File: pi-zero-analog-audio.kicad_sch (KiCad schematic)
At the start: 31 parts, among them J1 GPIO, J2 Screw_Terminal_01x04, J3 SJ1-3555NG-BE, U1 MIC5365-3.3YD5, U2 MC74VHC1GT50, U3 MC74VHC1GT50, U4 PAM8403D

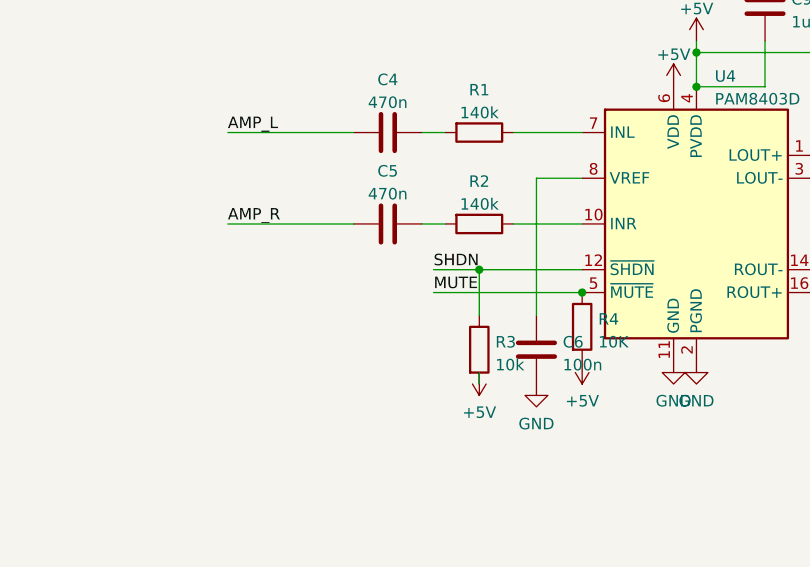
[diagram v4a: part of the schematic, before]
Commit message: Adding SolderJumpers for GPIO connections
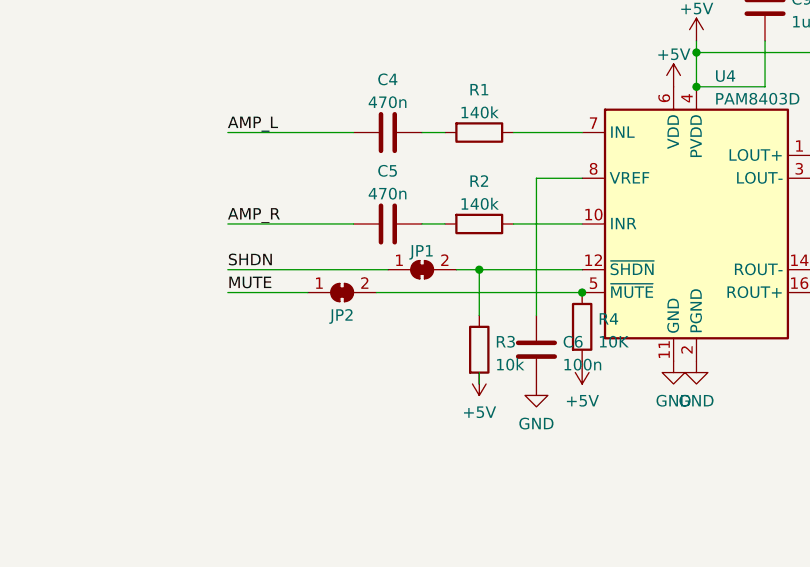
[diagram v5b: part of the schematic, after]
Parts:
- added JP1, JP2: SolderJumper_2_Bridged, Jumper:SolderJumper-2_P1.3mm_Bridged_RoundedPad1.0x1.5mm, symbol Jumper:SolderJumper_2_Bridged
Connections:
- net MUTE: now also JP2.1 (A); no longer R4.1, U4.5 (~{MUTE})
- net SHDN: now also JP1.1 (A); no longer R3.1, U4.12 (~{SHDN})
- new net: JP1.2 (B), R3.1, U4.12 (~{SHDN})
- new net: JP2.2 (B), R4.1, U4.5 (~{MUTE})
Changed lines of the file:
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@@
+    (stroke (width 0) (type default) (color 0 0 0 0))
+  )
+  (wire (pts (xy 101.6 134.62) (xy 104.14 134.62))
     (stroke (width 0) (type default) (color 0 0 0 0))
   )
@@
     (stroke (width 0) (type default) (color 0 0 0 0))
   )
-  (wire (pts (xy 99.06 137.16) (xy 115.57 137.16))
+  (wire (pts (xy 76.2 137.16) (xy 85.09 137.16))
     (stroke (width 0) (type default) (color 0 0 0 0))
   )
@@
     (stroke (width 0) (type solid) (color 0 0 0 0))
   )
-  (wire (pts (xy 99.06 134.62) (xy 104.14 134.62))
+  (wire (pts (xy 92.71 137.16) (xy 115.57 137.16))
+    (stroke (width 0) (type default) (color 0 0 0 0))
+  )
+  (wire (pts (xy 76.2 134.62) (xy 93.98 134.62))
     (stroke (width 0) (type default) (color 0 0 0 0))
   )
@@
     (effects (font (size 1.27 1.27)) (justify left bottom))
   )
-  (label "SHDN" (at 99.06 134.62 0)
+  (label "SHDN" (at 76.2 134.62 0)
     (effects (font (size 1.27 1.27)) (justify left bottom))
   )
@@
     (effects (font (size 1.27 1.27)) (justify left bottom))
   )
-  (label "MUTE" (at 99.06 137.16 0)
+  (label "MUTE" (at 76.2 137.16 0)
     (effects (font (size 1.27 1.27)) (justify left bottom))
   )
@@
   (symbol (lib_id "power:GND") (at 142.24 38.1 0) (unit 1)
     (in_bom yes) (on_board yes) (fields_autoplaced)
-    (property "Reference" "#PWR021" (id 0) (at 142.24 44.45 0)
+    (property "Reference" "#PWR022" (id 0) (at 142.24 44.45 0)
       (effects (font (size 1.27 1.27)) hide)
     )
@@
     (pin "1")
   )
+  (symbol (lib_id "Jumper:SolderJumper_2_Bridged") (at 97.79 134.62 0) (unit 1)
+    (in_bom yes) (on_board yes) (fields_autoplaced)
+    (property "Reference" "JP1" (id 0) (at 97.79 132.5682 0))
+    (property "Value" "SolderJumper_2_Bridged" (id 1) (at 97.79 132.5681 0)
+      (effects (font (size 1.27 1.27)) hide)
+    )
+    (property "Footprint" "Jumper:SolderJumper-2_P1.3mm_Bridged_RoundedPad1.0x1.5mm" (id 2) (at 97.79 134.62 0)
+      (effects (font (size 1.27 1.27)) hide)
+    )
+    (property "Datasheet" "~" (id 3) (at 97.79 134.62 0)
+      (effects (font (size 1.27 1.27)) hide)
+    )
+    (pin "1")
+    (pin "2")
+  )
   (symbol (lib_id "Device:C") (at 121.92 72.39 0) (unit 1)
     (in_bom yes) (on_board yes) (fields_autoplaced)
@@
   (symbol (lib_id "power:GND") (at 128.27 144.78 0) (unit 1)
     (in_bom yes) (on_board yes) (fields_autoplaced)
-    (property "Reference" "#PWR019" (id 0) (at 128.27 151.13 0)
+    (property "Reference" "#PWR020" (id 0) (at 128.27 151.13 0)
       (effects (font (size 1.27 1.27)) hide)
     )
@@
   (symbol (lib_id "power:+5V") (at 125.73 114.3 0) (unit 1)
     (in_bom yes) (on_board yes) (fields_autoplaced)
-    (property "Reference" "#PWR016" (id 0) (at 125.73 118.11 0)
+    (property "Reference" "#PWR017" (id 0) (at 125.73 118.11 0)
       (effects (font (size 1.27 1.27)) hide)
     )
@@
   (symbol (lib_id "power:+5V") (at 128.27 109.22 0) (unit 1)
     (in_bom yes) (on_board yes) (fields_autoplaced)
-    (property "Reference" "#PWR018" (id 0) (at 128.27 113.03 0)
+    (property "Reference" "#PWR019" (id 0) (at 128.27 113.03 0)
       (effects (font (size 1.27 1.27)) hide)
     )
@@
   (symbol (lib_id "power:GND") (at 201.93 41.91 0) (unit 1)
     (in_bom yes) (on_board yes) (fields_autoplaced)
-    (property "Reference" "#PWR026" (id 0) (at 201.93 48.26 0)
+    (property "Reference" "#PWR027" (id 0) (at 201.93 48.26 0)
       (effects (font (size 1.27 1.27)) hide)
     )
@@
   (symbol (lib_id "power:GND") (at 143.51 101.6 180) (unit 1)
     (in_bom yes) (on_board yes) (fields_autoplaced)
-    (property "Reference" "#PWR023" (id 0) (at 143.51 95.25 0)
+    (property "Reference" "#PWR024" (id 0) (at 143.51 95.25 0)
       (effects (font (size 1.27 1.27)) hide)
     )
@@
   (symbol (lib_id "power:GND") (at 143.51 73.66 0) (unit 1)
     (in_bom yes) (on_board yes) (fields_autoplaced)
-    (property "Reference" "#PWR022" (id 0) (at 143.51 80.01 0)
+    (property "Reference" "#PWR023" (id 0) (at 143.51 80.01 0)
       (effects (font (size 1.27 1.27)) hide)
     )
@@
   (symbol (lib_id "power:GND") (at 135.89 101.6 180) (unit 1)
     (in_bom yes) (on_board yes) (fields_autoplaced)
-    (property "Reference" "#PWR020" (id 0) (at 135.89 95.25 0)
+    (property "Reference" "#PWR021" (id 0) (at 135.89 95.25 0)
       (effects (font (size 1.27 1.27)) hide)
     )
@@
   (symbol (lib_id "power:GND") (at 161.29 73.66 0) (unit 1)
     (in_bom yes) (on_board yes) (fields_autoplaced)
-    (property "Reference" "#PWR025" (id 0) (at 161.29 80.01 0)
+    (property "Reference" "#PWR026" (id 0) (at 161.29 80.01 0)
       (effects (font (size 1.27 1.27)) hide)
     )
@@
   (symbol (lib_id "power:GND") (at 160.02 38.1 0) (unit 1)
     (in_bom yes) (on_board yes) (fields_autoplaced)
-    (property "Reference" "#PWR024" (id 0) (at 160.02 44.45 0)
+    (property "Reference" "#PWR025" (id 0) (at 160.02 44.45 0)
       (effects (font (size 1.27 1.27)) hide)
     )
@@
   (symbol (lib_id "power:GND") (at 125.73 144.78 0) (unit 1)
     (in_bom yes) (on_board yes) (fields_autoplaced)
-    (property "Reference" "#PWR017" (id 0) (at 125.73 151.13 0)
+    (property "Reference" "#PWR018" (id 0) (at 125.73 151.13 0)
       (effects (font (size 1.27 1.27)) hide)
     )
@@
     )
     (pin "1")
+  )
+  (symbol (lib_id "Jumper:SolderJumper_2_Bridged") (at 88.9 137.16 0) (unit 1)
+    (in_bom yes) (on_board yes)
+    (property "Reference" "JP2" (id 0) (at 88.9 139.7 0))
+    (property "Value" "SolderJumper_2_Bridged" (id 1) (at 88.9 135.1081 0)
+      (effects (font (size 1.27 1.27)) hide)
+    )
+    (property "Footprint" "Jumper:SolderJumper-2_P1.3mm_Bridged_RoundedPad1.0x1.5mm" (id 2) (at 88.9 137.16 0)
+      (effects (font (size 1.27 1.27)) hide)
+    )
+    (property "Datasheet" "~" (id 3) (at 88.9 137.16 0)
+      (effects (font (size 1.27 1.27)) hide)
+    )
+    (pin "1")
+    (pin "2")
   )
   (symbol (lib_id "Logic_LevelTranslator:SN74LV1T34DBV") (at 110.49 66.04 0) (unit 1)
@@
   (symbol (lib_id "power:GND") (at 121.92 76.2 0) (unit 1)
     (in_bom yes) (on_board yes) (fields_autoplaced)
-    (property "Reference" "#PWR0101" (id 0) (at 121.92 82.55 0)
+    (property "Reference" "#PWR016" (id 0) (at 121.92 82.55 0)
       (effects (font (size 1.27 1.27)) hide)
     )
@@
       (reference "#PWR015") (unit 1) (value "GND") (footprint "")
     )
+    (path "/ffede39b-8099-4955-86bd-53060798d5f3"
+      (reference "#PWR016") (unit 1) (value "GND") (footprint "")
+    )
     (path "/4da06035-fff1-4a29-81dd-8f4dbe59fff0"
-      (reference "#PWR016") (unit 1) (value "+5V") (footprint "")
+      (reference "#PWR017") (unit 1) (value "+5V") (footprint "")
     )
     (path "/e95beca7-444a-4cc5-9f40-709df3f136ab"
-      (reference "#PWR017") (unit 1) (value "GND") (footprint "")
+      (reference "#PWR018") (unit 1) (value "GND") (footprint "")
     )
     (path "/53e9b269-f0a7-47e4-af71-77298a928f0e"
-      (reference "#PWR018") (unit 1) (value "+5V") (footprint "")
+      (reference "#PWR019") (unit 1) (value "+5V") (footprint "")
     )
     (path "/4b95a9c2-acb6-4774-a3c3-7825fc03dabe"
-      (reference "#PWR019") (unit 1) (value "GND") (footprint "")
+      (reference "#PWR020") (unit 1) (value "GND") (footprint "")
     )
     (path "/b7024d58-cd8d-42b0-8d27-e41166a9a27b"
-      (reference "#PWR020") (unit 1) (value "GND") (footprint "")
+      (reference "#PWR021") (unit 1) (value "GND") (footprint "")
     )
     (path "/10e102fd-a91f-4c41-9a82-8c538dc349c6"
-      (reference "#PWR021") (unit 1) (value "GND") (footprint "")
+      (reference "#PWR022") (unit 1) (value "GND") (footprint "")
     )
     (path "/a31e2c62-695d-402d-aace-8193a0330673"
-      (reference "#PWR022") (unit 1) (value "GND") (footprint "")
+      (reference "#PWR023") (unit 1) (value "GND") (footprint "")
     )
     (path "/9efb607d-91e6-407b-8efc-00809228de63"
-      (reference "#PWR023") (unit 1) (value "GND") (footprint "")
+      (reference "#PWR024") (unit 1) (value "GND") (footprint "")
     )
     (path "/e13487f4-f7e8-42a5-aaa9-41aa8c3edf07"
-      (reference "#PWR024") (unit 1) (value "GND") (footprint "")
+      (reference "#PWR025") (unit 1) (value "GND") (footprint "")
     )
     (path "/d4eceaab-1d31-4003-bead-a40555a1f2ed"
-      (reference "#PWR025") (unit 1) (value "GND") (footprint "")
+      (reference "#PWR026") (unit 1) (value "GND") (footprint "")
     )
     (path "/78668128-17e5-44d7-9944-cfbf5034c0d3"
-      (reference "#PWR026") (unit 1) (value "GND") (footprint "")
-    )
-    (path "/ffede39b-8099-4955-86bd-53060798d5f3"
-      (reference "#PWR0101") (unit 1) (value "GND") (footprint "")
+      (reference "#PWR027") (unit 1) (value "GND") (footprint "")
     )
     (path "/e0d29500-3eeb-41c8-beba-a4e29bee1456"
@@
       (reference "J3") (unit 1) (value "SJ1-3555NG-BE") (footprint "library:CUI_SJ1-3555NG-BE")
     )
+    (path "/42de515a-bd7a-4b70-9fe9-9e1aed3ae372"
+      (reference "JP1") (unit 1) (value "SolderJumper_2_Bridged") (footprint "Jumper:SolderJumper-2_P1.3mm_Bridged_RoundedPad1.0x1.5mm")
+    )
+    (path "/ebb81792-e83d-4c58-b4ba-3ae00249565c"
+      (reference "JP2") (unit 1) (value "SolderJumper_2_Bridged") (footprint "Jumper:SolderJumper-2_P1.3mm_Bridged_RoundedPad1.0x1.5mm")
+    )
     (path "/d084b509-2bd2-4510-bb62-a6e63bec94c3"

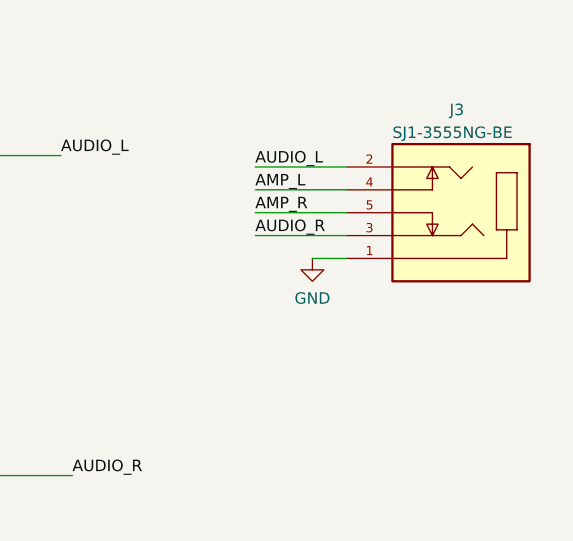
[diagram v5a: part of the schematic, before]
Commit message: Changing audio connector reference and footprint
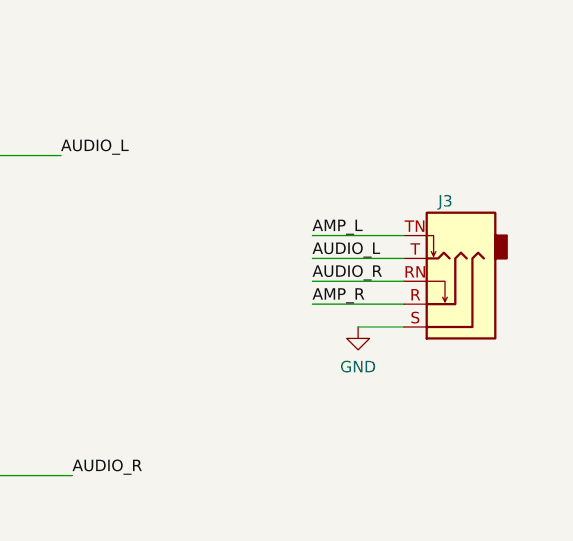
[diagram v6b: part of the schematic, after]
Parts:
- J3: value SJ1-3555NG-BE -> Audio Jack; footprint library:CUI_SJ1-3555NG-BE -> Connector_Audio:Jack_3.5mm_Ledino_KB3SPRS_Horizontal; symbol SJ1-3555NG-BE:SJ1-3555NG-BE -> Connector:AudioJack3_SwitchTR
- U1: footprint Package_TO_SOT_SMD:SOT-23-5 -> Package_TO_SOT_SMD:SOT-23-5_HandSoldering
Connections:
- net AMP_L: now also J3.TN; no longer J3.4
- net AMP_R: now also J3.R; no longer J3.5
- net AUDIO_L: now also J3.T; no longer J3.2
- net AUDIO_R: now also J3.RN; no longer J3.3
- net GND: now also J3.S; no longer J3.1
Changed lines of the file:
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@@
     (stroke (width 0) (type solid) (color 0 0 0 0))
   )
-  (wire (pts (xy 195.58 36.83) (xy 205.74 36.83))
+  (wire (pts (xy 201.93 46.99) (xy 212.09 46.99))
     (stroke (width 0) (type default) (color 0 0 0 0))
   )
@@
     (stroke (width 0) (type solid) (color 0 0 0 0))
   )
+  (wire (pts (xy 207.01 49.53) (xy 212.09 49.53))
+    (stroke (width 0) (type default) (color 0 0 0 0))
+  )
   (wire (pts (xy 87.63 30.48) (xy 87.63 33.02))
     (stroke (width 0) (type default) (color 0 0 0 0))
@@
     (stroke (width 0) (type default) (color 0 0 0 0))
   )
-  (wire (pts (xy 195.58 31.75) (xy 205.74 31.75))
+  (wire (pts (xy 201.93 41.91) (xy 212.09 41.91))
     (stroke (width 0) (type default) (color 0 0 0 0))
   )
@@
     (stroke (width 0) (type default) (color 0 0 0 0))
   )
-  (wire (pts (xy 195.58 39.37) (xy 205.74 39.37))
+  (wire (pts (xy 201.93 44.45) (xy 212.09 44.45))
     (stroke (width 0) (type default) (color 0 0 0 0))
   )
@@
     (stroke (width 0) (type default) (color 0 0 0 0))
   )
-  (wire (pts (xy 195.58 34.29) (xy 205.74 34.29))
+  (wire (pts (xy 201.93 39.37) (xy 212.09 39.37))
     (stroke (width 0) (type default) (color 0 0 0 0))
   )
@@
     (stroke (width 0) (type default) (color 0 0 0 0))
   )
-  (wire (pts (xy 205.74 41.91) (xy 201.93 41.91))
-    (stroke (width 0) (type default) (color 0 0 0 0))
-  )
   (text "Additional pin functions:\nhttps://pinout.xyz/" (at 179.07 180.34 0)
     (effects (font (size 1.27 1.27)) (justify left bottom))
@@
     (effects (font (size 1.27 1.27)) (justify left bottom))
   )
-  (label "AUDIO_R" (at 195.58 39.37 0)
+  (label "AUDIO_R" (at 201.93 44.45 0)
     (effects (font (size 1.27 1.27)) (justify left bottom))
   )
@@
     (effects (font (size 1.27 1.27)) (justify left bottom))
   )
-  (label "AMP_R" (at 195.58 36.83 0)
+  (label "AMP_R" (at 201.93 46.99 0)
     (effects (font (size 1.27 1.27)) (justify left bottom))
   )
@@
     (effects (font (size 1.27 1.27)) (justify left bottom))
   )
-  (label "AMP_L" (at 195.58 34.29 0)
+  (label "AMP_L" (at 201.93 39.37 0)
     (effects (font (size 1.27 1.27)) (justify left bottom))
   )
@@
     (effects (font (size 1.27 1.27)) (justify left bottom))
   )
-  (label "AUDIO_L" (at 195.58 31.75 0)
+  (label "AUDIO_L" (at 201.93 41.91 0)
     (effects (font (size 1.27 1.27)) (justify left bottom))
   )
@@
     (pin "2")
   )
-  (symbol (lib_id "SJ1-3555NG-BE:SJ1-3555NG-BE") (at 218.44 36.83 180) (unit 1)
+  (symbol (lib_id "Connector:AudioJack3_SwitchTR") (at 217.17 46.99 180) (unit 1)
     (in_bom yes) (on_board yes)
-    (property "Reference" "J3" (id 0) (at 217.17 25.4 0)
+    (property "Reference" "J3" (id 0) (at 215.9 35.56 0)
       (effects (font (size 1.27 1.27)) (justify right))
     )
-    (property "Value" "SJ1-3555NG-BE" (id 1) (at 210.82 27.94 0)
-      (effects (font (size 1.27 1.27)) (justify right))
-    )
-    (property "Footprint" "library:CUI_SJ1-3555NG-BE" (id 2) (at 218.44 36.83 0)
+    (property "Value" "Audio Jack" (id 1) (at 212.09 38.1 0)
+      (effects (font (size 1.27 1.27)) (justify right) hide)
+    )
+    (property "Footprint" "Connector_Audio:Jack_3.5mm_Ledino_KB3SPRS_Horizontal" (id 2) (at 217.17 46.99 0)
+      (effects (font (size 1.27 1.27)) hide)
+    )
+    (property "Datasheet" "~" (id 3) (at 217.17 46.99 0)
+      (effects (font (size 1.27 1.27)) hide)
+    )
+    (property "MANUFACTURER" "CUI Devices" (id 4) (at 217.17 46.99 0)
       (effects (font (size 1.27 1.27)) (justify left bottom) hide)
     )
-    (property "Datasheet" "" (id 3) (at 218.44 36.83 0)
+    (property "PART_REV" "1.0" (id 5) (at 217.17 46.99 0)
       (effects (font (size 1.27 1.27)) (justify left bottom) hide)
     )
-    (property "MANUFACTURER" "CUI Devices" (id 4) (at 218.44 36.83 0)
+    (property "SNAPEDA_PN" "SJ1-3555NG-BE" (id 6) (at 217.17 46.99 0)
       (effects (font (size 1.27 1.27)) (justify left bottom) hide)
     )
-    (property "PART_REV" "1.0" (id 5) (at 218.44 36.83 0)
+    (property "STANDARD" "Manufacturer Recommendation" (id 7) (at 217.17 46.99 0)
       (effects (font (size 1.27 1.27)) (justify left bottom) hide)
     )
-    (property "SNAPEDA_PN" "SJ1-3555NG-BE" (id 6) (at 218.44 36.83 0)
+    (property "MAXIMUM_PACKAGE_HEIGHT" "10.3 mm" (id 8) (at 217.17 46.99 0)
       (effects (font (size 1.27 1.27)) (justify left bottom) hide)
     )
-    (property "STANDARD" "Manufacturer Recommendation" (id 7) (at 218.44 36.83 0)
-      (effects (font (size 1.27 1.27)) (justify left bottom) hide)
-    )
-    (property "MAXIMUM_PACKAGE_HEIGHT" "10.3 mm" (id 8) (at 218.44 36.83 0)
-      (effects (font (size 1.27 1.27)) (justify left bottom) hide)
-    )
-    (pin "1")
-    (pin "2")
-    (pin "3")
-    (pin "4")
-    (pin "5")
+    (pin "R")
+    (pin "RN")
+    (pin "S")
+    (pin "T")
+    (pin "TN")
   )
   (symbol (lib_id "Device:R") (at 160.02 34.29 0) (unit 1)
@@
     (pin "2")
   )
-  (symbol (lib_id "power:GND") (at 201.93 41.91 0) (unit 1)
-    (in_bom yes) (on_board yes) (fields_autoplaced)
-    (property "Reference" "#PWR027" (id 0) (at 201.93 48.26 0)
-      (effects (font (size 1.27 1.27)) hide)
-    )
-    (property "Value" "GND" (id 1) (at 201.93 46.3534 0))
-    (property "Footprint" "" (id 2) (at 201.93 41.91 0)
-      (effects (font (size 1.27 1.27)) hide)
-    )
-    (property "Datasheet" "" (id 3) (at 201.93 41.91 0)
+  (symbol (lib_id "power:GND") (at 207.01 49.53 0) (unit 1)
+    (in_bom yes) (on_board yes) (fields_autoplaced)
+    (property "Reference" "#PWR027" (id 0) (at 207.01 55.88 0)
+      (effects (font (size 1.27 1.27)) hide)
+    )
+    (property "Value" "GND" (id 1) (at 207.01 53.9734 0))
+    (property "Footprint" "" (id 2) (at 207.01 49.53 0)
+      (effects (font (size 1.27 1.27)) hide)
+    )
+    (property "Datasheet" "" (id 3) (at 207.01 49.53 0)
       (effects (font (size 1.27 1.27)) hide)
     )
@@
     (property "Reference" "U1" (id 0) (at 72.39 24.2402 0))
     (property "Value" "MIC5365-3.3YD5" (id 1) (at 72.39 26.7771 0))
-    (property "Footprint" "Package_TO_SOT_SMD:SOT-23-5" (id 2) (at 72.39 24.13 0)
+    (property "Footprint" "Package_TO_SOT_SMD:SOT-23-5_HandSoldering" (id 2) (at 72.39 24.13 0)
       (effects (font (size 1.27 1.27)) hide)
     )
@@
     )
     (path "/0b4362dd-e0ca-493b-8fc1-107bd0984034"
-      (reference "J3") (unit 1) (value "SJ1-3555NG-BE") (footprint "library:CUI_SJ1-3555NG-BE")
+      (reference "J3") (unit 1) (value "Audio Jack") (footprint "Connector_Audio:Jack_3.5mm_Ledino_KB3SPRS_Horizontal")
     )
     (path "/42de515a-bd7a-4b70-9fe9-9e1aed3ae372"
@@
     )
     (path "/8e6d6488-458c-4211-a3e8-dc13acff85e7"
-      (reference "U1") (unit 1) (value "MIC5365-3.3YD5") (footprint "Package_TO_SOT_SMD:SOT-23-5")
+      (reference "U1") (unit 1) (value "MIC5365-3.3YD5") (footprint "Package_TO_SOT_SMD:SOT-23-5_HandSoldering")
     )
     (path "/a8cd6fe4-3274-461b-a92b-74b79798d756"

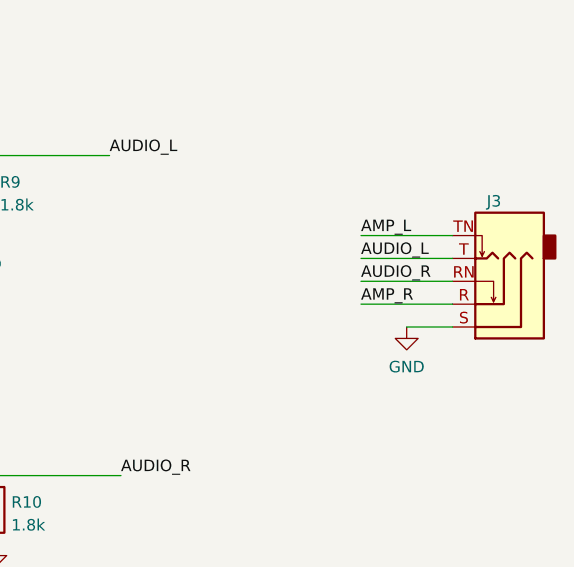
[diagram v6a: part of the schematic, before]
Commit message: Fix error in audio jack
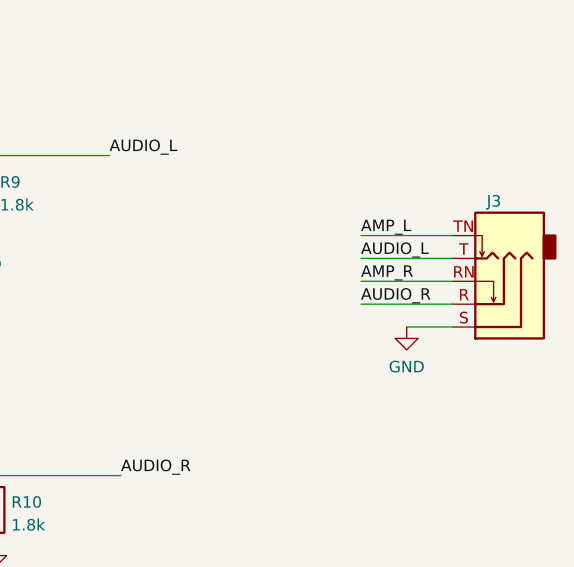
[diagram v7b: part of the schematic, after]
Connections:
- net AMP_R: now also J3.RN; no longer J3.R
- net AUDIO_R: now also J3.R; no longer J3.RN
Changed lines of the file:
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@@
-    (effects (font (size 1.27 1.27)) (justify left bottom))
-  )
-  (label "AUDIO_R" (at 201.93 44.45 0)
     (effects (font (size 1.27 1.27)) (justify left bottom))
   )
   (label "AMP_L" (at 76.2 119.38 0)
+    (effects (font (size 1.27 1.27)) (justify left bottom))
+  )
+  (label "AMP_R" (at 201.93 44.45 0)
     (effects (font (size 1.27 1.27)) (justify left bottom))
   )
@@
   )
   (label "L+" (at 162.56 129.54 0)
-    (effects (font (size 1.27 1.27)) (justify left bottom))
-  )
-  (label "AMP_R" (at 201.93 46.99 0)
     (effects (font (size 1.27 1.27)) (justify left bottom))
   )
@@
     (effects (font (size 1.27 1.27)) (justify left bottom))
   )
+  (label "AUDIO_R" (at 201.93 46.99 0)
+    (effects (font (size 1.27 1.27)) (justify left bottom))
+  )
